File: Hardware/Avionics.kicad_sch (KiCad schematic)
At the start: 64 parts, among them J1 DX07S016JA1R1500, J2 SWD, J3 LiPo 4s, J4 Qwiic, J5 PS-562Q, J6 DM3AT-SF-PEJM5, J7 XD-3420, Q1 BSS138, SW1 ~{RESET}, SW2 ~{BOOT}, U1 W25Q128JVS, U2 RP2040, U3 NCP1117-3.3, U4 DRV8870DDA, U5 LSM6DSO32, Y1 12MHz

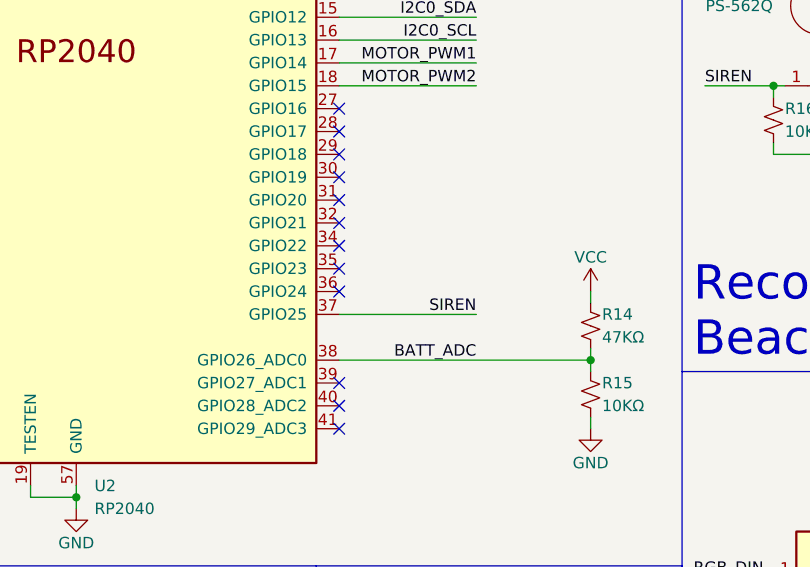
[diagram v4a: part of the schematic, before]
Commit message: Moved reference designators to fab layer
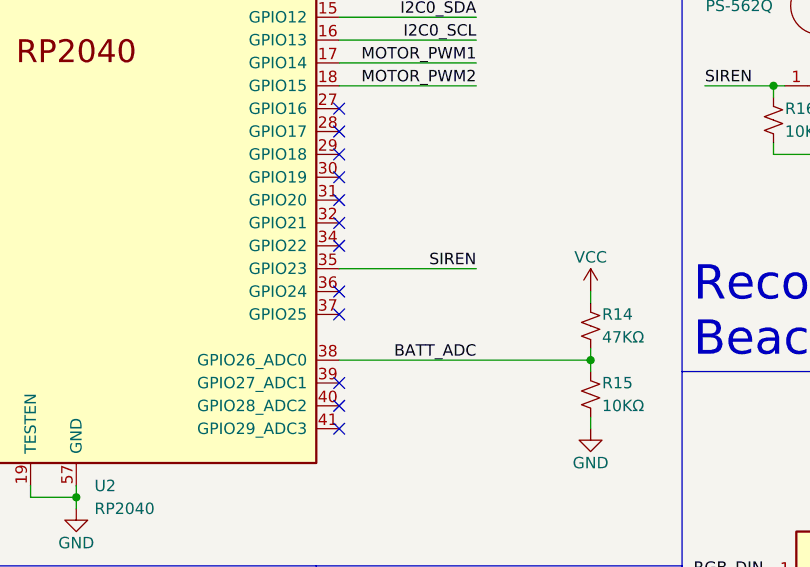
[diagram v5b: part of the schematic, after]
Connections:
- net SIREN: now also U2.35 (GPIO23); no longer U2.37 (GPIO25)
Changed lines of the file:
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@@
   (junction (at 121.92 27.94) (diameter 0) (color 0 0 0 0)
   )
+  (no_connect (at 120.65 115.57))
   (no_connect (at 40.64 180.34))
   (no_connect (at 40.64 182.88))
@@
   (no_connect (at 184.15 144.78))
   (no_connect (at 120.65 52.07))
-  (no_connect (at 120.65 110.49))
   (wire (pts (xy 205.74 151.13) (xy 217.17 151.13))
     (stroke (width 0) (type default) (color 0 0 0 0))
@@
     (stroke (width 0) (type default) (color 0 0 0 0))
   )
+  (wire (pts (xy 135.89 110.49) (xy 120.65 110.49))
+    (stroke (width 0) (type default) (color 0 0 0 0))
+  )
   (wire (pts (xy 135.89 90.17) (xy 120.65 90.17))
     (stroke (width 0) (type default) (color 0 0 0 0))
@@
     (stroke (width 0) (type default) (color 0 0 0 0))
   )
-  (wire (pts (xy 135.89 115.57) (xy 120.65 115.57))
-    (stroke (width 0) (type default) (color 0 0 0 0))
-  )
   (wire (pts (xy 110.49 27.94) (xy 121.92 27.94))
     (stroke (width 0) (type default) (color 0 0 0 0))
@@
     (effects (font (size 1.27 1.27)) (justify right bottom))
   )
+  (label "SIREN" (at 135.89 110.49 180)
+    (effects (font (size 1.27 1.27)) (justify right bottom))
+  )
   (label "BATT_ADC" (at 135.89 120.65 180)
     (effects (font (size 1.27 1.27)) (justify right bottom))
@@
     (effects (font (size 1.27 1.27)) (justify right bottom))
   )
-  (label "SIREN" (at 135.89 115.57 180)
-    (effects (font (size 1.27 1.27)) (justify right bottom))
-  )
